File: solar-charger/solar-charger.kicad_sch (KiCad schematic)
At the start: 11 parts, among them IC1 TLV809EA30DBZR, IC2 TLV803EB33VDBZR, J1 Conn_01x02_solar_cell, J2 Conn_01x02_battery, J3 Conn_01x02_to_ESP32_voltage_r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, Q1 AO3415, Q2 AO3416

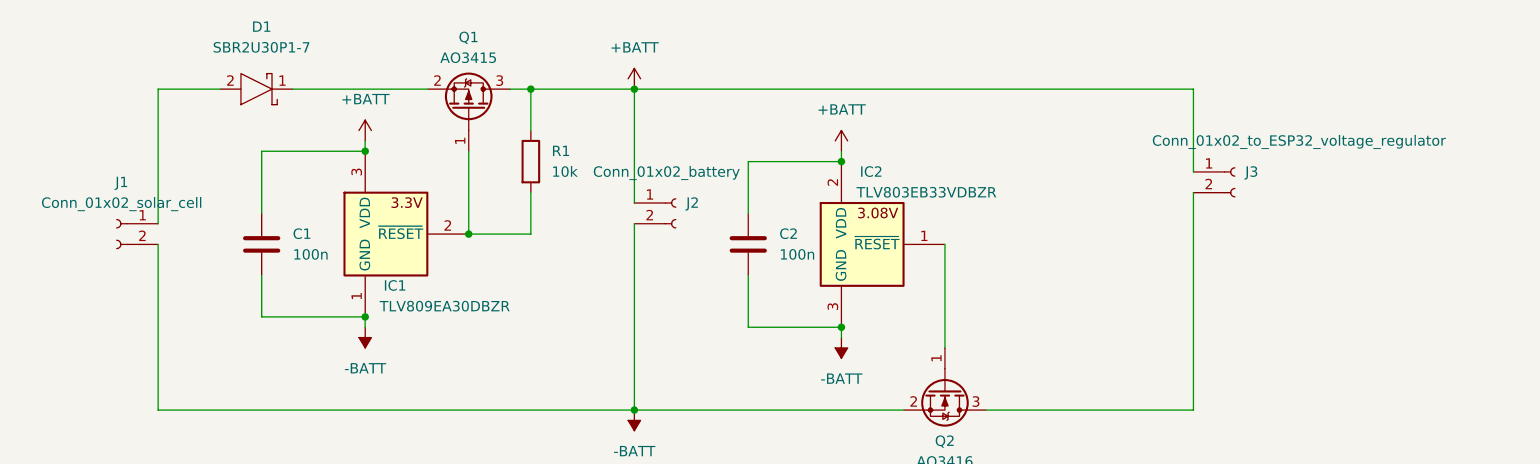
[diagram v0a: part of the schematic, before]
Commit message: Add personal part library and update
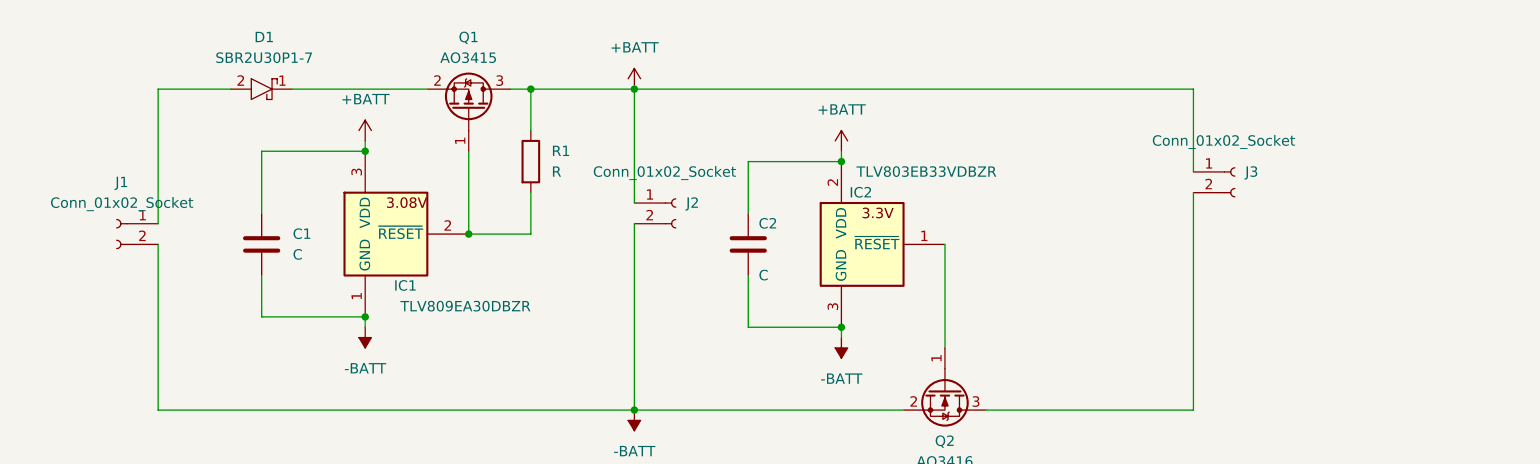
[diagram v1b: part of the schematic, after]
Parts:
- removed D1: SBR2U30P1-7, Marcus_Library:SODFL3718X100N, symbol Marcus_Library:SBR2U30P1-7
- removed IC1: TLV809EA30DBZR, Marcus_Library:SOT95P237X95-3N, symbol Marcus_Library:TLV809EA30DBZR
- removed IC2: TLV803EB33VDBZR, Marcus_Library:SOT95P237X112-3N, symbol Marcus_Library:TLV803EB33VDBZR
- removed Q1: AO3415, Package_TO_SOT_SMD:SOT-23, symbol Marcus_IC_library:AO3415
- removed Q2: AO3416, Package_TO_SOT_SMD:SOT-23, symbol Marcus_IC_library:AO3416
- added D1: SBR2U30P1-7, Marcus-PCB-Library:SODFL3718X100N, symbol Marcus-PCB-Library:SBR2U30P1-7
- added IC1: TLV809EA30DBZR, Marcus_Library:SOT95P237X95-3N, symbol Marcus-PCB-Library:TLV809EA30DBZR
- added IC2: TLV803EB33VDBZR, Marcus_Library:SOT95P237X112-3N, symbol Marcus-PCB-Library:TLV803EB33VDBZR
- added Q1: AO3415, SOT95P280X125-3N, symbol Marcus-PCB-Library:AO3415
- added Q2: AO3416, Package_TO_SOT_SMD:SOT-23, symbol Marcus-PCB-Library:AO3416
- C1, C2: value 100n -> C
- J1: value Conn_01x02_solar_cell -> Conn_01x02_Socket
- J2: value Conn_01x02_battery -> Conn_01x02_Socket
- J3: value Conn_01x02_to_ESP32_voltage_regulator -> Conn_01x02_Socket
- R1: value 10k -> R
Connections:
- net +BATT: now also IC1.3 (VDD), IC2.2 (VDD), Q1.3 (D)
- net -BATT: now also IC1.1 (GND), IC2.3 (GND), Q2.2 (S)
- net at R1.2: now also IC1.2 (~{RESET}), Q1.1 (G)
- net at J3.2 (Pin_2): now also Q2.3 (D)
- net at J1.1 (Pin_1): now also D1.2 (A)
- new net: D1.1 (K), Q1.2 (S)
- new net: IC2.1 (~{RESET}), Q2.1 (G)

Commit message: finish 1. working PCB
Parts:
- removed C2: C, Capacitor_SMD:C_0805_2012Metric_Pad1.18x1.45mm_HandSolder, symbol Device:C
- removed IC1: TLV809EA30DBZR, Marcus_Library:SOT95P237X95-3N, symbol Marcus-PCB-Library:TLV809EA30DBZR
- removed IC2: TLV803EB33VDBZR, Marcus_Library:SOT95P237X112-3N, symbol Marcus-PCB-Library:TLV803EB33VDBZR
- removed J1, J2, J3: Conn_01x02_Socket, Connector_PinHeader_1.27mm:PinHeader_1x02_P1.27mm_Vertical, symbol Connector:Conn_01x02_Socket
- removed Q2: AO3416, Package_TO_SOT_SMD:SOT-23, symbol Marcus-PCB-Library:AO3416
- added IC1: TPS3700DDCR, Marcus-PCB-Library:SOT98P280X110-6N, symbol Marcus-PCB-Library:TPS3700DDCR
- added J1: Solar Cell, Marcus-PCB-Library:10129378902001BLF, symbol Marcus-PCB-Library:2x-Header-Pin-Through-Hole
- added J2: Battery, Marcus-PCB-Library:10129378902001BLF, symbol Marcus-PCB-Library:2x-Header-Pin-Through-Hole
- added J3: power out, Marcus-PCB-Library:10129378902001BLF, symbol Marcus-PCB-Library:2x-Header-Pin-Through-Hole
- added Q2: AO3415, Package_TO_SOT_SMD:SOT-23, symbol Marcus-PCB-Library:AO3415
- added R2: 51k, Resistor_SMD:R_0805_2012Metric_Pad1.20x1.40mm_HandSolder, symbol Device:R
- added R3, R5: 470k, Resistor_SMD:R_0805_2012Metric_Pad1.20x1.40mm_HandSolder, symbol Device:R
- added R4, R6: 33k, Resistor_SMD:R_0805_2012Metric_Pad1.20x1.40mm_HandSolder, symbol Device:R
- added VR1, VR2: 50k, Marcus-PCB-Library:TC33X2104E, symbol Marcus-PCB-Library:TC33X-trimmer
- C1: value C -> 100nF
- Q1: footprint SOT95P280X125-3N -> Package_TO_SOT_SMD:SOT-23
- R1: value R -> 51k
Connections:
- net +BATT: now also IC1.5 (VDD), J2.1, Q2.2 (S), R2.1, R3.1, R5.1; no longer R1.1
- net -BATT: now also IC1.2 (GND), J1.2, J2.2, J3.2, VR1.2 (WIPER), VR2.2 (WIPER)
- net at D1.2 (A): now also R1.1, J1.1
- net at Q1.1 (G), R1.2: now also IC1.1 (OUTA)
- new net: J3.1, Q2.3 (D)
- new net: IC1.3 (INA+), R3.2, R4.1
- new net: IC1.6 (OUTB), Q2.1 (G), R2.2
- new net: R4.2, VR1.3 (CW)
- new net: IC1.4 (INB-), R5.2, R6.1
- new net: R6.2, VR2.3 (CW)
- no-connect marks 0 -> 2
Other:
- moved on the sheet: C1, D1

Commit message: Save
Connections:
- net -BATT: now also VR1.1 (CCW), VR2.3 (CW)
- net at R6.2: now also VR2.1 (CCW); no longer VR2.3 (CW)
- no-connect marks 2 -> 0
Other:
- note added: "27,71k"
- note added: "34,8k"
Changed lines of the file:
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@@
 	(generator_version "9.0")
 	(paper "A4")
+	(text "27,71k"
+		(exclude_from_sim no)
+		(at 58.42 92.71 0)
+		(effects
+			(font
+				(size 1.27 1.27)
+			)
+		)
+	)
+	(text "34,8k"
+		(exclude_from_sim no)
+		(at 71.12 92.71 0)
+		(effects
+			(font
+				(size 1.27 1.27)
+			)
+		)
+	)
 	(junction
 		(at 119.38 58.42)
@@
 	)
 	(junction
+		(at 58.42 104.14)
+		(diameter 0)
+		(color 0 0 0 0)
+	)
+	(junction
 		(at 90.17 82.55)
+		(diameter 0)
+		(color 0 0 0 0)
+	)
+	(junction
+		(at 71.12 104.14)
 		(diameter 0)
 		(color 0 0 0 0)
@@
 		(color 0 0 0 0)
 	)
-	(no_connect
-		(at 67.31 104.14)
-	)
-	(no_connect
-		(at 54.61 104.14)
-	)
 	(wire
 		(pts
@@
 	(wire
 		(pts
-			(xy 71.12 97.79) (xy 71.12 109.22)
+			(xy 71.12 97.79) (xy 71.12 104.14)
 		)
 		(stroke
@@
 	(wire
 		(pts
+			(xy 58.42 104.14) (xy 58.42 109.22)
+		)
+		(stroke
+			(width 0)
+			(type default)
+		)
+	)
+	(wire
+		(pts
 			(xy 102.87 69.85) (xy 119.38 69.85)
 		)
@@
 	(wire
 		(pts
+			(xy 54.61 104.14) (xy 58.42 104.14)
+		)
+		(stroke
+			(width 0)
+			(type default)
+		)
+	)
+	(wire
+		(pts
 			(xy 67.31 52.07) (xy 67.31 54.61)
 		)
@@
 	(wire
 		(pts
-			(xy 58.42 97.79) (xy 58.42 109.22)
+			(xy 58.42 97.79) (xy 58.42 104.14)
 		)
 		(stroke
@@
 	(wire
 		(pts
+			(xy 67.31 104.14) (xy 71.12 104.14)
+		)
+		(stroke
+			(width 0)
+			(type default)
+		)
+	)
+	(wire
+		(pts
 			(xy 219.71 49.53) (xy 219.71 62.23)
 		)
@@
 		(pts
 			(xy 67.31 86.36) (xy 67.31 91.44)
+		)
+		(stroke
+			(width 0)
+			(type default)
+		)
+	)
+	(wire
+		(pts
+			(xy 71.12 104.14) (xy 71.12 109.22)
 		)
 		(stroke
@@
 		(lib_id "Marcus-PCB-Library:TC33X-trimmer")
 		(at 67.31 97.79 0)
+		(mirror x)
 		(unit 1)
 		(exclude_from_sim no)
@@
 		(dnp no)
 		(property "Reference" "VR2"
-			(at 64.77 91.44 0)
+			(at 64.77 104.14 0)
 			(effects
 				(font
@@
 		)
 		(property "Value" "50k"
-			(at 64.77 93.98 0)
+			(at 64.77 101.6 0)
 			(effects
 				(font
@@
 		)
 		(property "Footprint" "Marcus-PCB-Library:TC33X2104E"
-			(at 76.2 200.33 0)
+			(at 76.2 -4.75 0)
 			(effects
 				(font
@@
 		)
 		(property "Datasheet" "https://www.bourns.com/docs/Product-Datasheets/TC33.pdf"
-			(at 76.2 300.33 0)
+			(at 76.2 -104.75 0)
 			(effects
 				(font
@@
 		)
 		(property "Description" "Trimmer Resistors - SMD 3MM 25% 0.1WATT OPEN FRM"
-			(at 71.12 89.535 0)
+			(at 71.12 106.045 0)
 			(effects
 				(font
@@
 		)
 		(property "Height" "1.5"
-			(at 76.2 500.33 0)
+			(at 76.2 -304.75 0)
 			(effects
 				(font
@@
 		)
 		(property "Mouser Part Number" "652-TC33X-2-104E"
-			(at 76.2 600.33 0)
+			(at 76.2 -404.75 0)
 			(effects
 				(font
@@
 		)
 		(property "Mouser Price/Stock" "https://www.mouser.co.uk/ProductDetail/Bourns/TC33X-2-104E?qs=2hAPiALdQ0llyX8B3WfcDg%3D%3D"
-			(at 76.2 700.33 0)
+			(at 76.2 -504.75 0)
 			(effects
 				(font
@@
 		)
 		(property "Manufacturer_Name" "Bourns"
-			(at 76.2 800.33 0)
+			(at 76.2 -604.75 0)
 			(effects
 				(font
@@
 		)
 		(property "Manufacturer_Part_Number" "TC33X-2-104E"
-			(at 76.2 900.33 0)
-			(effects
-				(font
+			(at 76.2 -704.75 0)
+			(effects
+				(font

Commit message: Save
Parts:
- R1, R2: value 51k -> 470k
- R3, R5: value 470k -> 680k
- R4: value 33k -> 51k
- R6: value 33k -> 75k
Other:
- moved on the sheet: C1, D1, IC1, J1, J2, J3, Q1, Q2, R1, R2, R3, R4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
